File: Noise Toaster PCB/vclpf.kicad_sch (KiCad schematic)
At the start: 16 parts, among them J7 VCLPF, Q5 2N5457, U2 LM324

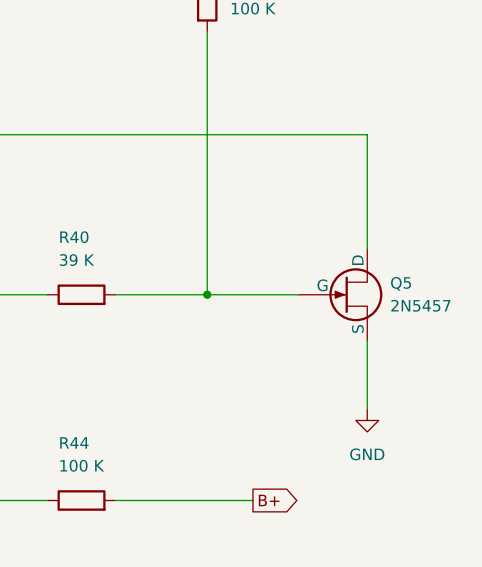
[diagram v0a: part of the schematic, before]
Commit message: added front panel pcb
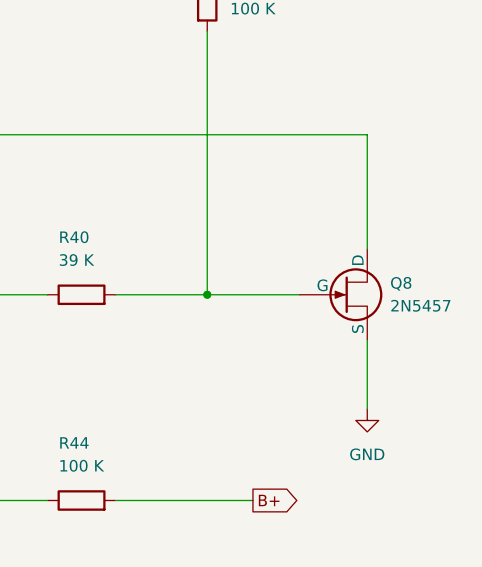
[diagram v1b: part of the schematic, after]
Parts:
- renumbered Q5 to Q8
